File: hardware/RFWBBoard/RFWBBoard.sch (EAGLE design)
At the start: 89 parts, among them IC1 24LC025ST, J1 CON-71742-3003-BOT, M1 MOUNT-HOLE3.3, M2 MOUNT-HOLE3.3, M3 MOUNT-HOLE3.3, M4 MOUNT-HOLE3.3, U1 MAX2830IPC-7351, U2 LDB212G4010C-001, U3 LDB212G4010C-001, U4 AD8132MSOP8, U5 AD8132MSOP8, U6 AD8132MSOP8, U7 AD8132MSOP8, X1 LTI-SASF54GT, X2 LTI-SASF54GT, X4 LTI-SASF54GT, X5 LTI-SASF54GT, X6 LTI-SASF54GT, X7 LTI-SASF54GT

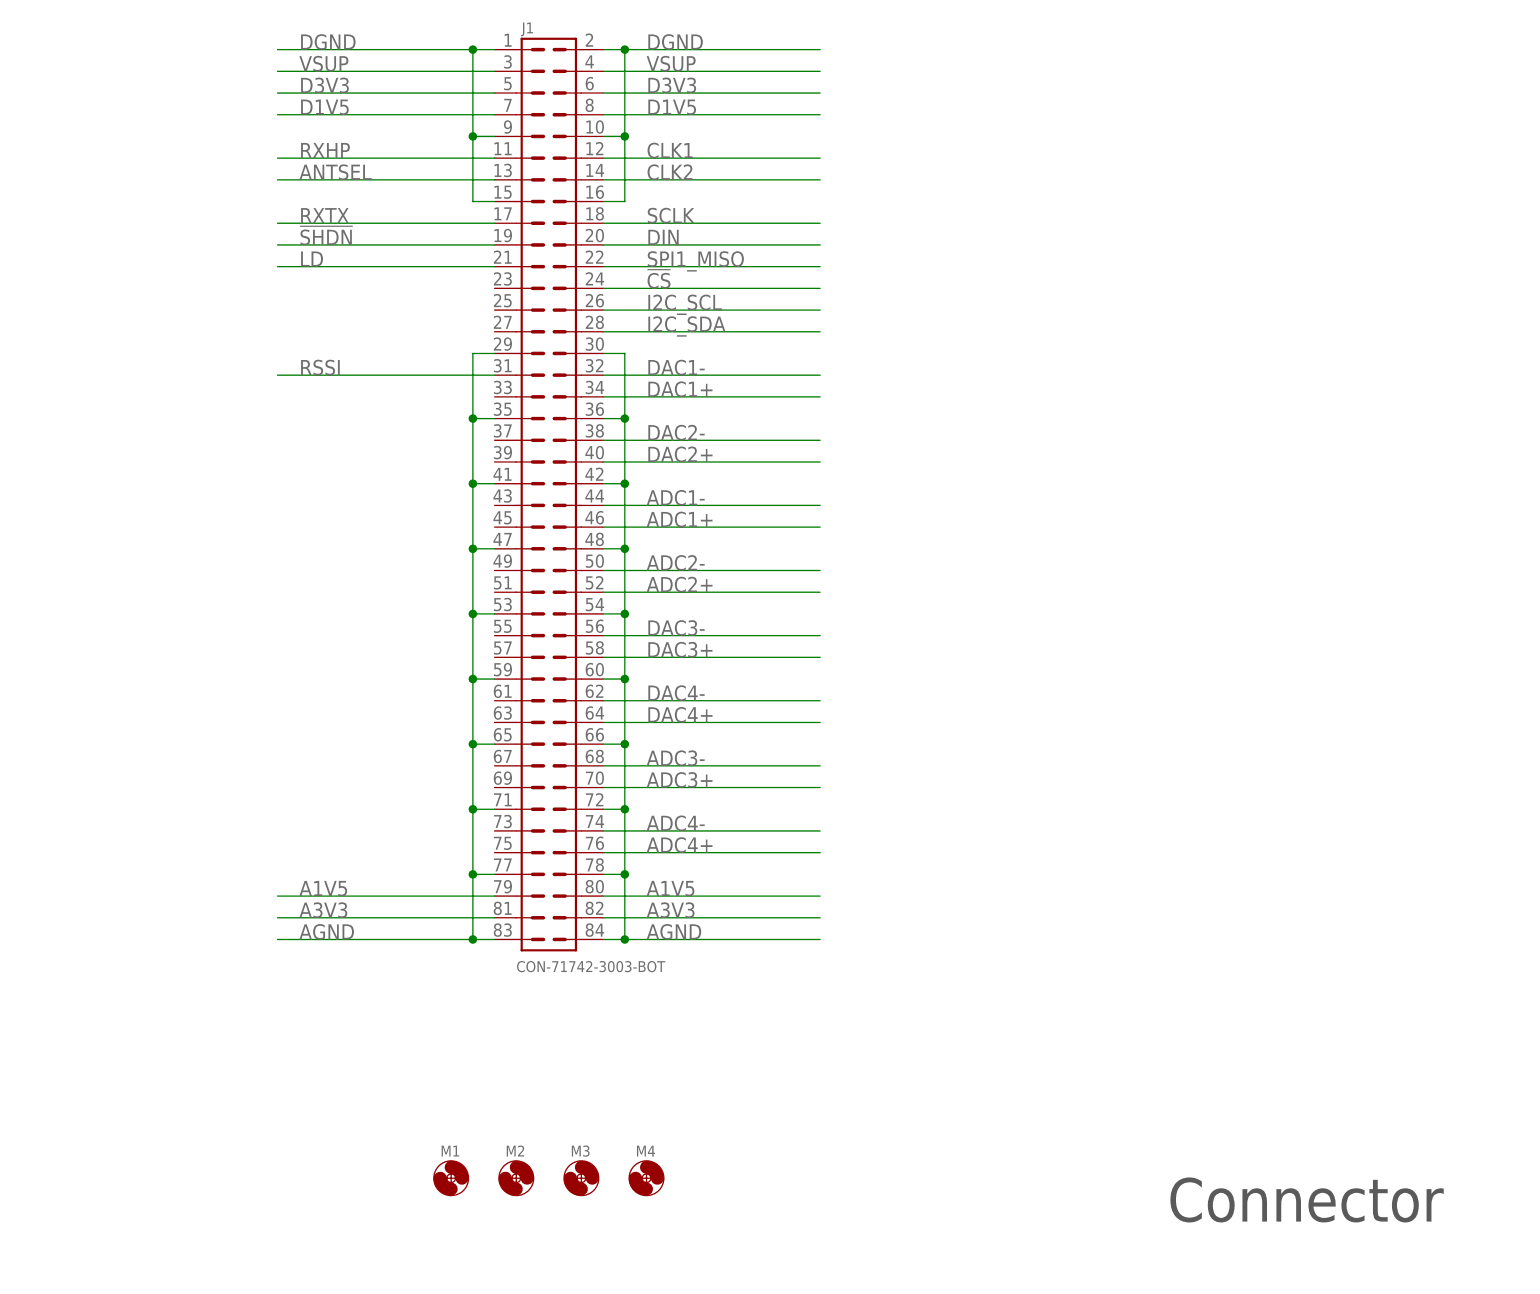
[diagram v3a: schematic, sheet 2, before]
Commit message: - Layout update - Interface update (RSSI -> SF_ADC6)
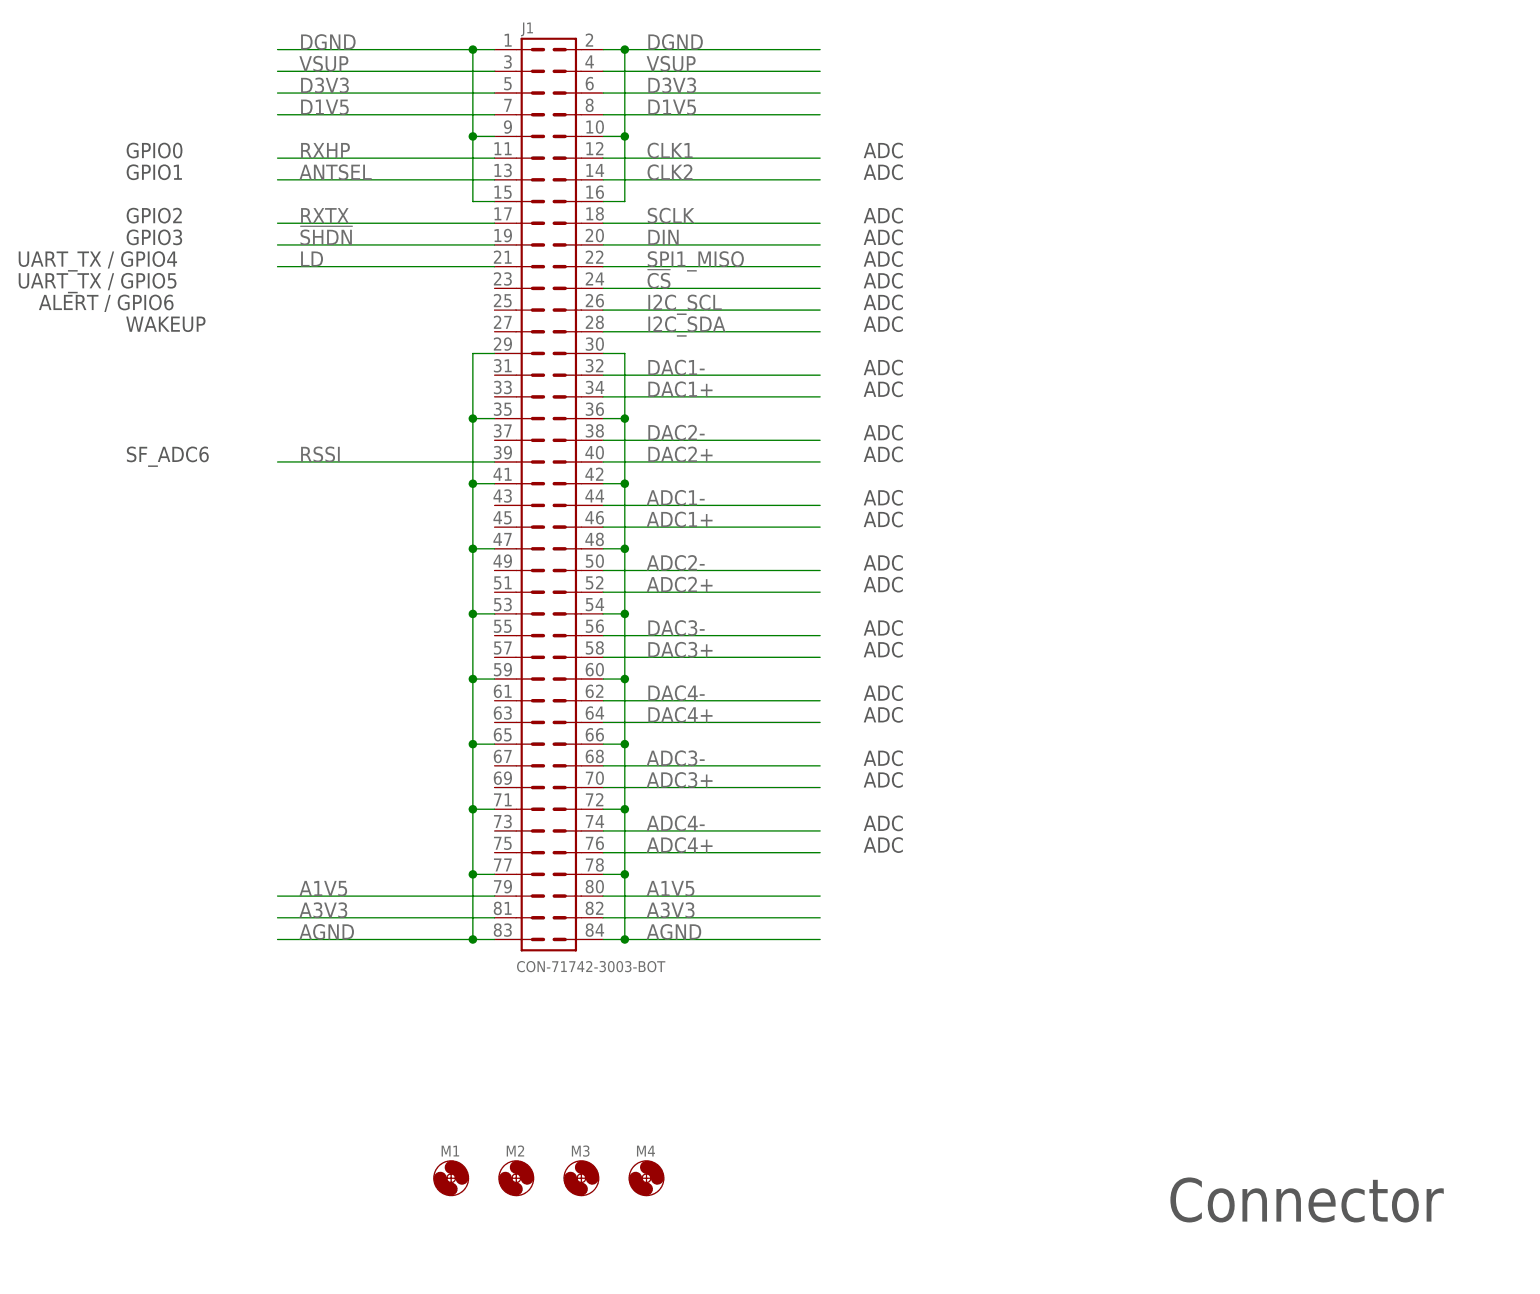
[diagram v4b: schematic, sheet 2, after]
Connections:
- net RSSI: now also J1.39; no longer J1.31
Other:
- note added: "ADC"
- note added: "ALERT / GPIO6"
- note added: "GPIO0"
- note added: "GPIO1"
- note added: "GPIO2"
- note added: "GPIO3"
- note added: "SF_ADC6"
- note added: "UART_TX / GPIO4"
- note added: "UART_TX / GPIO5"
- note added: "WAKEUP"
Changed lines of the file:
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@@
 <plain>
 <text x="190.5" y="20.32" size="5.08" layer="97">&gt;PAGE2</text>
+<text x="68.58" y="109.22" size="1.778" layer="97">SF_ADC6</text>
+<text x="68.58" y="137.16" size="1.778" layer="97">GPIO2</text>
+<text x="68.58" y="134.62" size="1.778" layer="97">GPIO3</text>
+<text x="68.58" y="142.24" size="1.778" layer="97">GPIO1</text>
+<text x="68.58" y="144.78" size="1.778" layer="97">GPIO0</text>
+<text x="55.88" y="132.08" size="1.778" layer="97">UART_TX / GPIO4</text>
+<text x="154.94" y="137.16" size="1.778" layer="97">ADC</text>
+<text x="154.94" y="134.62" size="1.778" layer="97">ADC</text>
+<text x="154.94" y="132.08" size="1.778" layer="97">ADC</text>
+<text x="154.94" y="129.54" size="1.778" layer="97">ADC</text>
+<text x="154.94" y="127" size="1.778" layer="97">ADC</text>
+<text x="154.94" y="124.46" size="1.778" layer="97">ADC</text>
+<text x="154.94" y="119.38" size="1.778" layer="97">ADC</text>
+<text x="154.94" y="116.84" size="1.778" layer="97">ADC</text>
+<text x="154.94" y="111.76" size="1.778" layer="97">ADC</text>
+<text x="154.94" y="109.22" size="1.778" layer="97">ADC</text>
+<text x="154.94" y="104.14" size="1.778" layer="97">ADC</text>
+<text x="154.94" y="101.6" size="1.778" layer="97">ADC</text>
+<text x="154.94" y="96.52" size="1.778" layer="97">ADC</text>
+<text x="154.94" y="93.98" size="1.778" layer="97">ADC</text>
+<text x="154.94" y="88.9" size="1.778" layer="97">ADC</text>
+<text x="154.94" y="86.36" size="1.778" layer="97">ADC</text>
+<text x="154.94" y="81.28" size="1.778" layer="97">ADC</text>
+<text x="154.94" y="78.74" size="1.778" layer="97">ADC</text>
+<text x="154.94" y="73.66" size="1.778" layer="97">ADC</text>
+<text x="154.94" y="71.12" size="1.778" layer="97">ADC</text>
+<text x="154.94" y="66.04" size="1.778" layer="97">ADC</text>
+<text x="154.94" y="63.5" size="1.778" layer="97">ADC</text>
+<text x="154.94" y="144.78" size="1.778" layer="97">ADC</text>
+<text x="154.94" y="142.24" size="1.778" layer="97">ADC</text>
+<text x="55.88" y="129.54" size="1.778" layer="97">UART_TX / GPIO5</text>
+<text x="58.42" y="127" size="1.778" layer="97">ALERT / GPIO6</text>
+<text x="68.58" y="124.46" size="1.778" layer="97">WAKEUP</text>
 </plain>
 <instances>
@@
 <net name="RSSI" class="0">
 <segment>
-<wire x1="111.76" y1="119.38" x2="86.36" y2="119.38" width="0.1524" layer="91"/>
-<label x="88.9" y="119.38" size="1.778" layer="95"/>
-<pinref part="J1" gate="G$1" pin="31"/>
-</segment>
-</net>
+<wire x1="111.76" y1="109.22" x2="86.36" y2="109.22" width="0.1524" layer="91"/>
+<label x="88.9" y="109.22" size="1.778" layer="95"/>
+<pinref part="J1" gate="G$1" pin="39"/>
+</segment>
+</net>

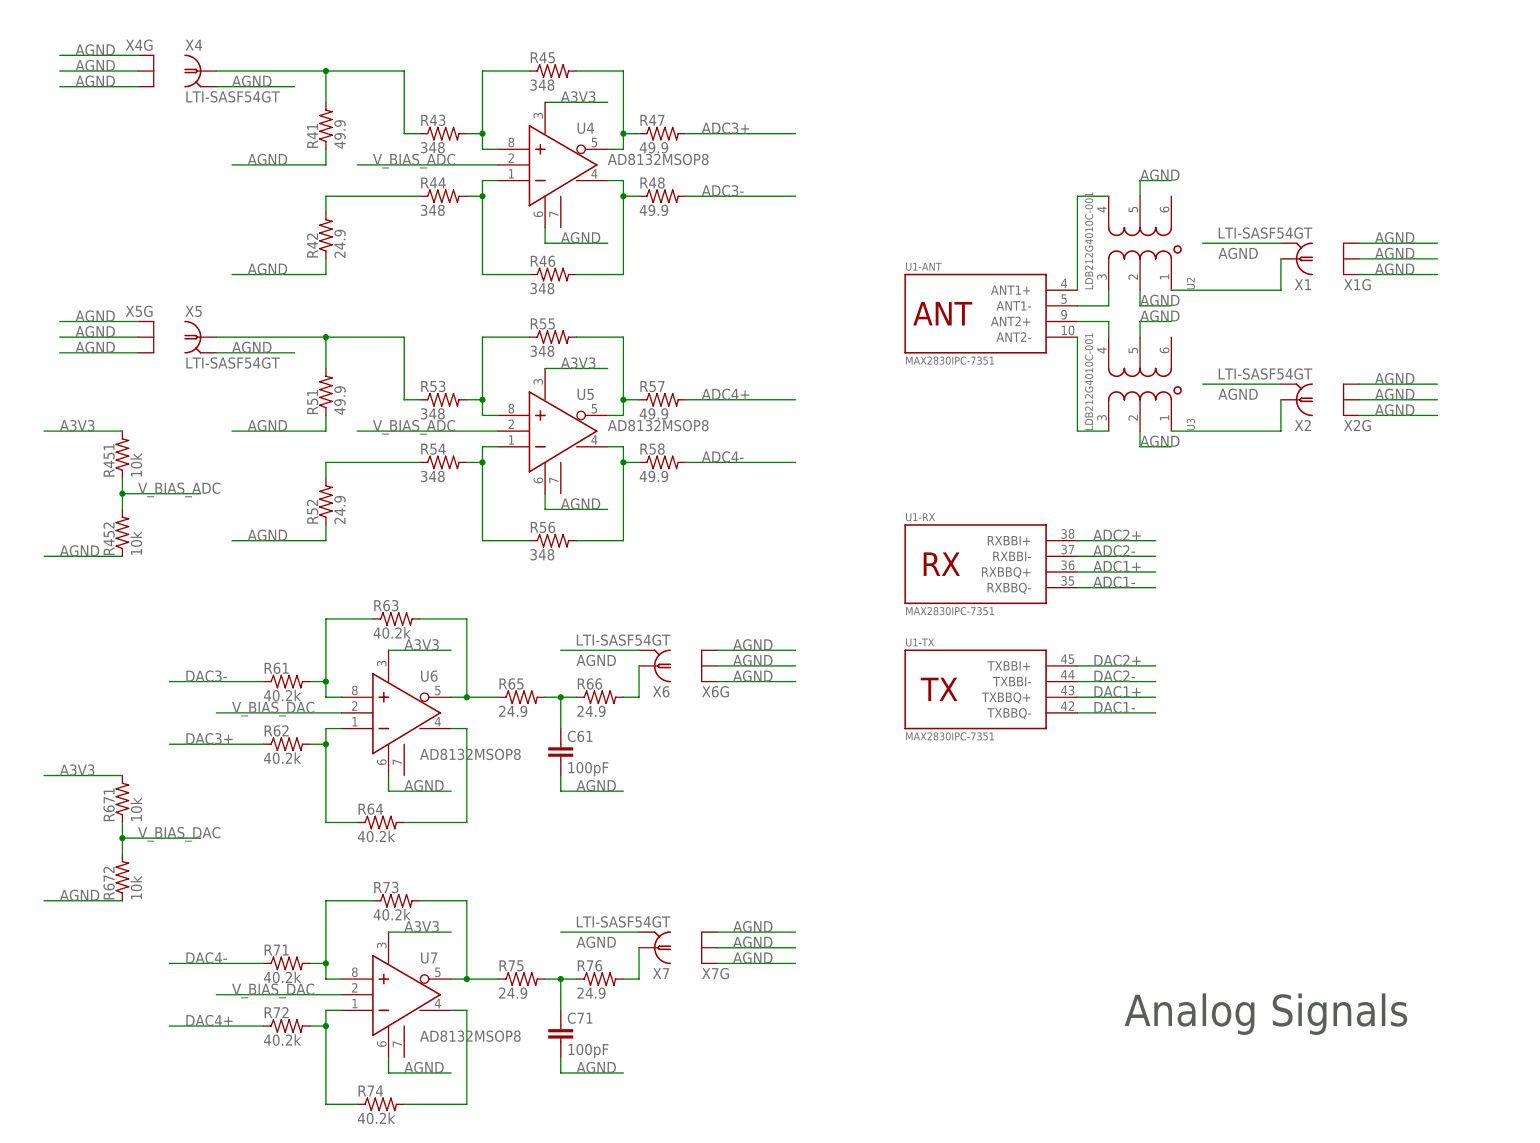
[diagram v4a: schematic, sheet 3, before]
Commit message: - Layout update - Oscillator added
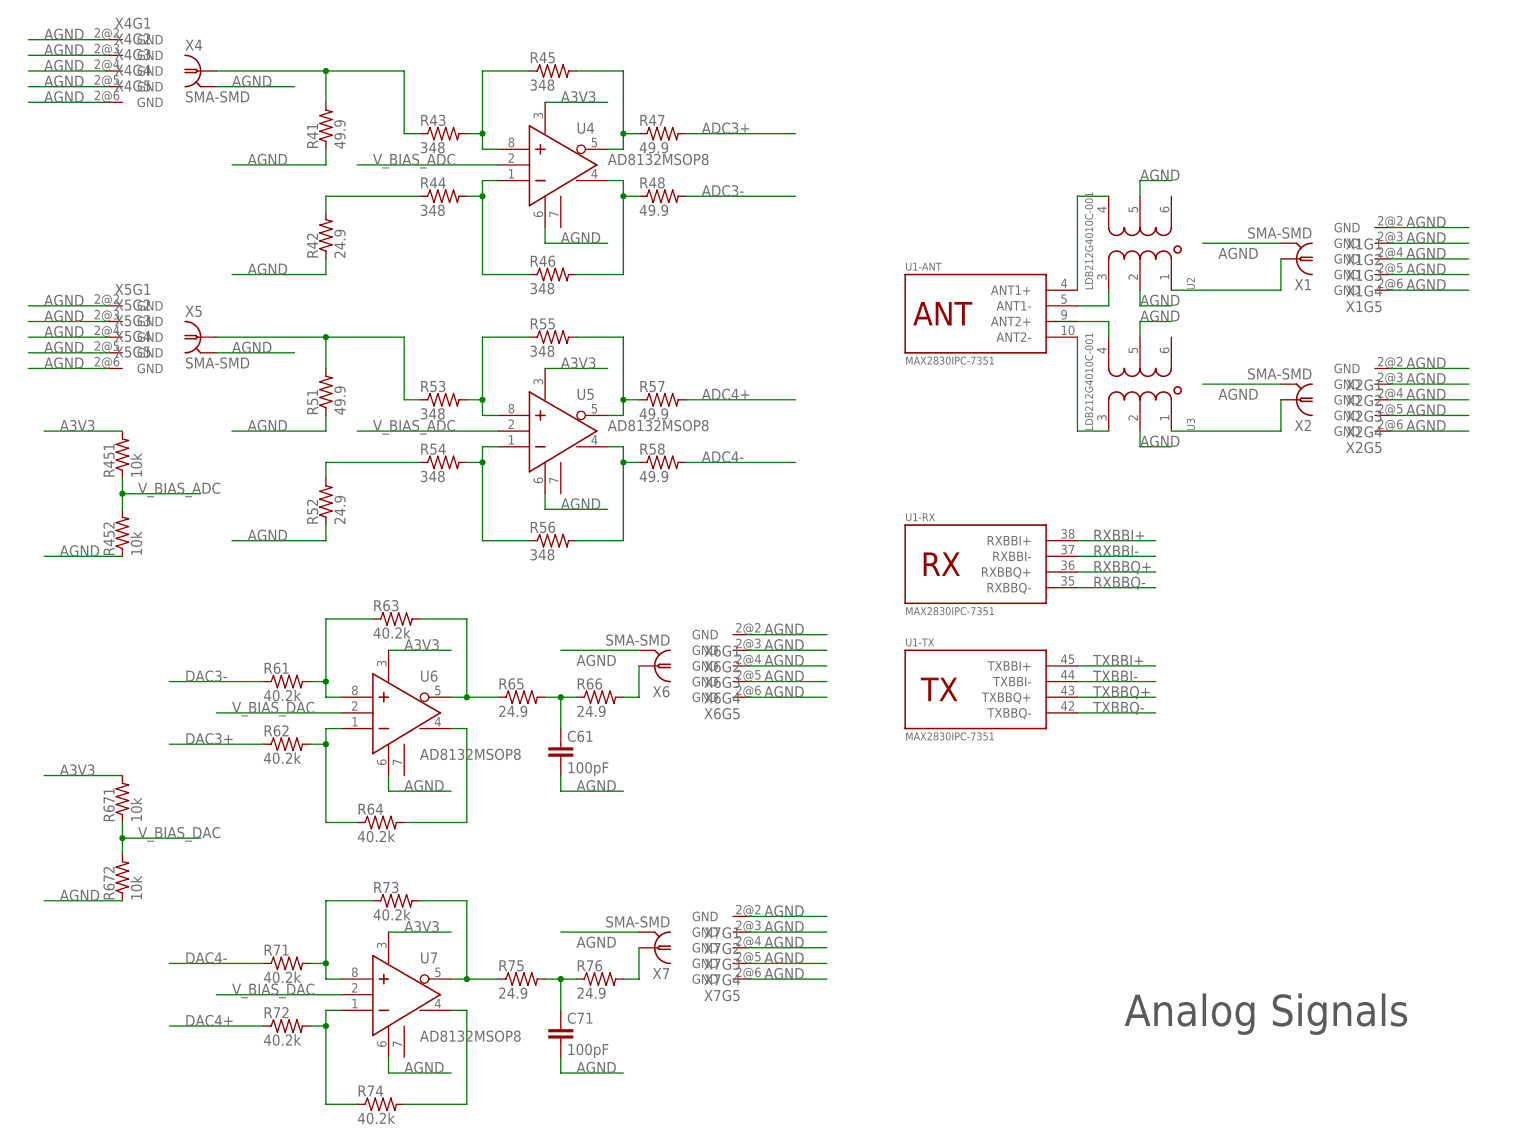
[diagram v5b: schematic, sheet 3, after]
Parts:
- added M5, M6, M7, M8: FIDUCIAL1X2, RFWBBoard:FIDUCIAL1X2
- added U8: LMV112, RFWBBoard:LMV112
- added X3: FOX924B, RFWBBoard:FOX924B
- X1, X2, X4, X5: value LTI-SASF54GT -> SMA-SMD; device RFWBBoard:LTI-SASF54GT -> RFWBBoard:SMA-SMD
- X6, X7: value LTI-SASF54GT -> SMA-SMD; device RFWBBoard:LTI-SASF54GT -> RFWBBoard:SMA-SMD; OC_FARNELL unknown -> (none); OC_NEWARK unknown -> (none)
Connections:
- net ADC1+ renamed RXBBQ+
- net ADC1- renamed RXBBQ-
- net ADC2+ renamed RXBBI+
- net ADC2- renamed RXBBI-
- net DAC1+ renamed TXBBQ+
- net DAC1- renamed TXBBQ-
- net DAC2+ renamed TXBBI+
- net DAC2- renamed TXBBI-
- removed net SPI1_MISO: J1.22
- new net N$36: C121.2, X3.FO
- net A3V3: now also X3.VCC
- net AGND: now also X1G1.GND, X1G2.GND, X1G3.GND, X1G4.GND, X1G5.GND, X2G1.GND, X2G2.GND, X2G3.GND, X2G4.GND, X2G5.GND, X3.GND, X4G1.GND, X4G2.GND, X4G3.GND, X4G4.GND, X4G5.GND, X5G1.GND, X5G2.GND, X5G3.GND, X5G4.GND, X5G5.GND, X6G1.GND, X6G2.GND, X6G3.GND, X6G4.GND, X6G5.GND, X7G1.GND, X7G2.GND, X7G3.GND, X7G4.GND, X7G5.GND; no longer X1G.GND@1, X1G.GND@2, X1G.GND@3, X2G.GND@1, X2G.GND@2, X2G.GND@3, X4G.GND@1, X4G.GND@2, X4G.GND@3, X5G.GND@1, X5G.GND@2, X5G.GND@3, X6G.GND@1, X6G.GND@2, X6G.GND@3, X7G.GND@1, X7G.GND@2, X7G.GND@3
- net CLK1: no longer C121.2
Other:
- note added: "ADC1+"
- note added: "ADC1-"
- note added: "ADC2+"
- note added: "ADC2-"
- note added: "ADC3+"
- note added: "ADC3-"
- note added: "ADC4+"
- note added: "ADC4-"
- note added: "DAC1+"
- note added: "DAC1-"
- note added: "DAC2+"
- note added: "DAC2-"
- note added: "DAC3+"
- note added: "DAC3-"
- note added: "DAC4+"
- note added: "DAC4-"
- note added: "I2C_SCL"
- note added: "REF_CLK+"
- note added: "REF_CLK-"
- note added: "SF_ABPS0"
- note added: "SF_ABPS1"
- note added: "SF_ADC0"
- note added: "SF_ADC1"
- note added: "SF_ADC2"
- note added: "SF_ADC3"
- note added: "SF_ADC4"
- note added: "SF_ADC5"
- note added: "SF_ADC7"
- note added: "SF_CM0"
- note added: "SF_CM1"
- note added: "SF_DAC0"
- note added: "SF_DAC1"
- note added: "SF_TM0"
- note added: "SF_TM1"
- note added: "SPI_MISO"
- note added: "SPI_MOSI"
- note added: "SPI_SCLK"
- note added: "SPI_SS"
- note removed: "ADC"
- moved on the sheet: C121

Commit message: - Layout update
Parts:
- added C122: 1000pF, RFWBBoard:C0402
- added C123, C126, C129: 10uF, RFWBBoard:C0805
- added C124, C127, C130: 100nF, RFWBBoard:C0402
- added C125, C128, C131: 100pF, RFWBBoard:C0402
- added U9: ICS85320I, RFWBBoard:ICS85320I
- U8: value LMV112 -> ICS83021I; device RFWBBoard:LMV112 -> RFWBBoard:ICS83021I
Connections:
- new net N$37: J1.11
- new net N$38: J1.13
- new net N$39: C122.1, U9.CLK
- new net N$40: J1.23
- new net N$41: J1.19
- new net N$42: J1.21
- net !SHDN: no longer J1.19
- net A3V3: now also C123.1, C124.1, C125.1, C126.1, C127.1, C128.1, C129.1, C130.1, C131.1, U8.VDD, U9.VCC
- net AGND: now also C123.2, C124.2, C125.2, C126.2, C127.2, C128.2, C129.2, C130.2, C131.2, U8.GND, U9.VEE
- net ANTSEL: no longer J1.13
- net CLK1: now also U8.CLK, U9.Q
- net CLK2: now also U8.NCLK, U9.NQ
- net LD: no longer J1.21
- net N$36: now also C122.2, U8.Q0
- net RXHP: no longer J1.11
- net RXTX: no longer J1.17
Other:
- note added: "either or"
- moved on the sheet: C103, C104, C105, C106, C107, C108, C109, C110, C111, C112, C113, C114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

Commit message: - Decoupling capacitors - Layout update - Schematic update
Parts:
- added C41, C51: 10uF, RFWBBoard:CPOL2012
- added C42, C45, C52, C62, C67, C72: 100nF, RFWBBoard:C0402
- added C43, C53, C63, C73: 10nF, RFWBBoard:C0402
- added C64, C74: 100pF, RFWBBoard:C0402
- added R3, R4: DNP, RFWBBoard:R0603
- C61, C71: value 100pF -> 10uF; device RFWBBoard:C0402 -> RFWBBoard:CPOL2012
- RA00, RA01, RA10, RA11, RA20, RA21, RWP0, RWP1: value NONE -> DNP
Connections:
- removed net N$37: J1.11
- removed net N$38: J1.13
- removed net N$40: J1.23
- removed net N$41: J1.19
- removed net N$42: J1.21
- net !SHDN: now also J1.13
- net A3V3: now also C41.+, C42.1, C43.1, C51.+, C52.1, C53.1, C61.+, C62.1, C63.1, C71.+, C72.1, C73.1
- net AGND: now also C41.-, C42.2, C43.2, C45.2, C51.-, C52.2, C53.2, C61.-, C62.2, C63.2, C64.2, C67.2, C71.-, C72.2, C73.2, C74.2, R3.2, R4.2; no longer C61.2, C71.2
- net ANTSEL: now also J1.19
- net DGND: now also R3.1, R4.1
- net LD: now also J1.11
- net N$27: now also C64.1; no longer C61.1
- net N$33: now also C74.1; no longer C71.1
- net RXHP: now also J1.17
- net RXTX: now also J1.21
- net V_BIAS_ADC: now also C45.1
- net V_BIAS_DAC: now also C67.1
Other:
- note added: "50 Ohm"
- note added: "RX"
- note added: "TX"
- note added: "either"
- note added: "or"
- note removed: "either or"
